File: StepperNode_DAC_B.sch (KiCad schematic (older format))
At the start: 0 parts

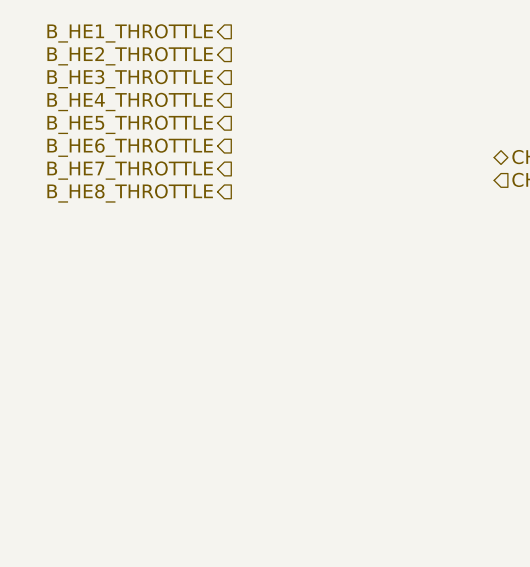
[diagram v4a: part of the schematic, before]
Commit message: Added Aux Prop Interface Sheet
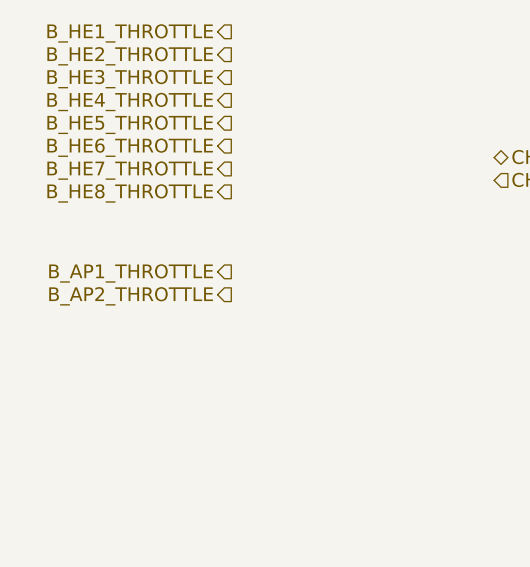
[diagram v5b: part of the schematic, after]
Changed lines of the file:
@@
 $Descr A3 16535 11693
 encoding utf-8
-Sheet 6 14
+Sheet 6 16
 Title "DAC Channel B"
 Date ""
@@
 Text HLabel 2950 3850 2    60   Input ~ 0
 CHB_DAC_NCNVT
+Text HLabel 1800 5200 0    60   Output ~ 0
+B_AP1_THROTTLE
+Text HLabel 1800 5300 0    60   Output ~ 0
+B_AP2_THROTTLE
 $EndSCHEMATC

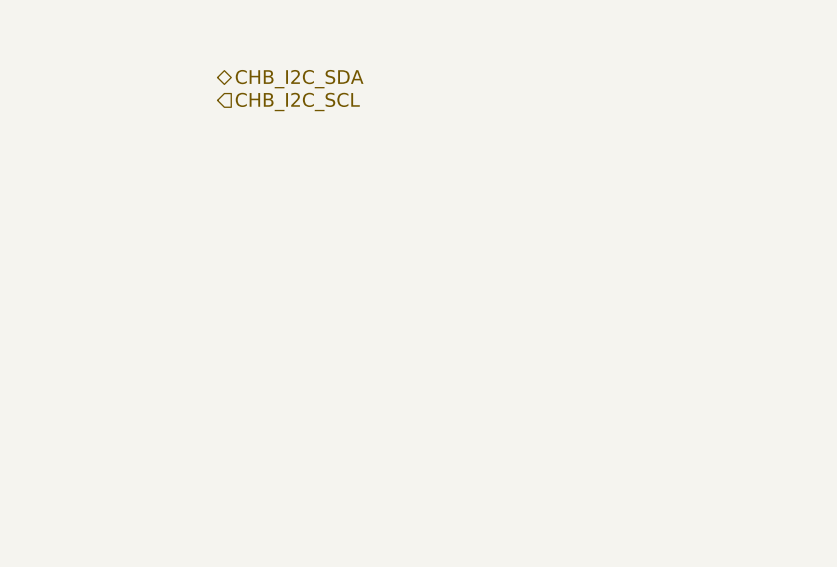
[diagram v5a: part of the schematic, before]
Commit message: Added sheet for Stepper Motor RTD temp sensors.
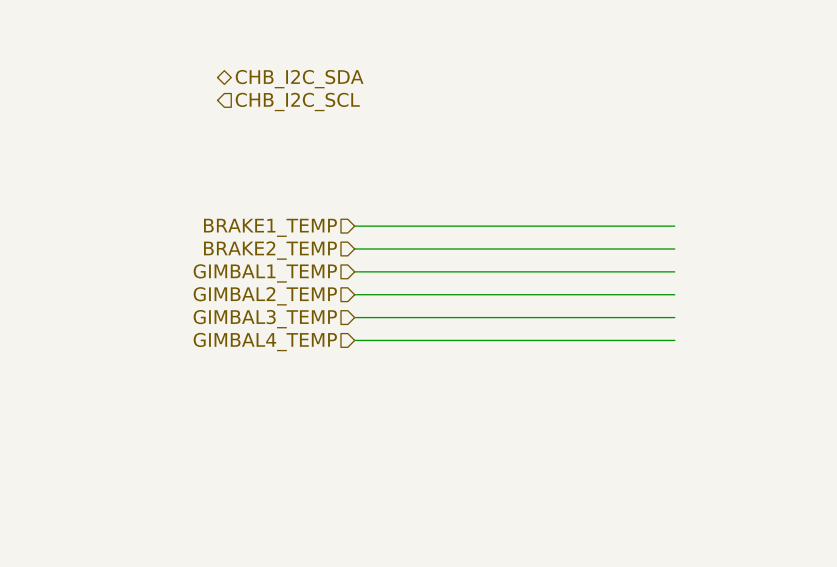
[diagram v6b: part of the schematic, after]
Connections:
- net labels added: BRAKE1_TEMP, BRAKE2_TEMP, GIMBAL1_TEMP, GIMBAL2_TEMP, GIMBAL3_TEMP, GIMBAL4_TEMP
- wire segments 0 -> 6
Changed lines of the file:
@@
 LIBS:microcontrollers
 LIBS:dsp
-LIBS:microchip
 LIBS:analog_switches
 LIBS:motorola
@@
 $Descr A3 16535 11693
 encoding utf-8
-Sheet 6 16
+Sheet 5 17
 Title "DAC Channel B"
 Date ""
@@
 Text HLabel 1800 5300 0    60   Output ~ 0
 B_AP2_THROTTLE
+Wire Wire Line
+	4950 5350 3550 5350
+Text HLabel 3550 5350 0    60   Input ~ 0
+BRAKE1_TEMP
+Wire Wire Line
+	4950 5450 3550 5450
+Text HLabel 3550 5450 0    60   Input ~ 0
+BRAKE2_TEMP
+Wire Wire Line
+	4950 5550 3550 5550
+Text HLabel 3550 5550 0    60   Input ~ 0
+GIMBAL1_TEMP
+Wire Wire Line
+	4950 5650 3550 5650
+Text HLabel 3550 5650 0    60   Input ~ 0
+GIMBAL2_TEMP
+Wire Wire Line
+	4950 5750 3550 5750
+Text HLabel 3550 5750 0    60   Input ~ 0
+GIMBAL3_TEMP
+Wire Wire Line
+	4950 5850 3550 5850
+Text HLabel 3550 5850 0    60   Input ~ 0
+GIMBAL4_TEMP
 $EndSCHEMATC

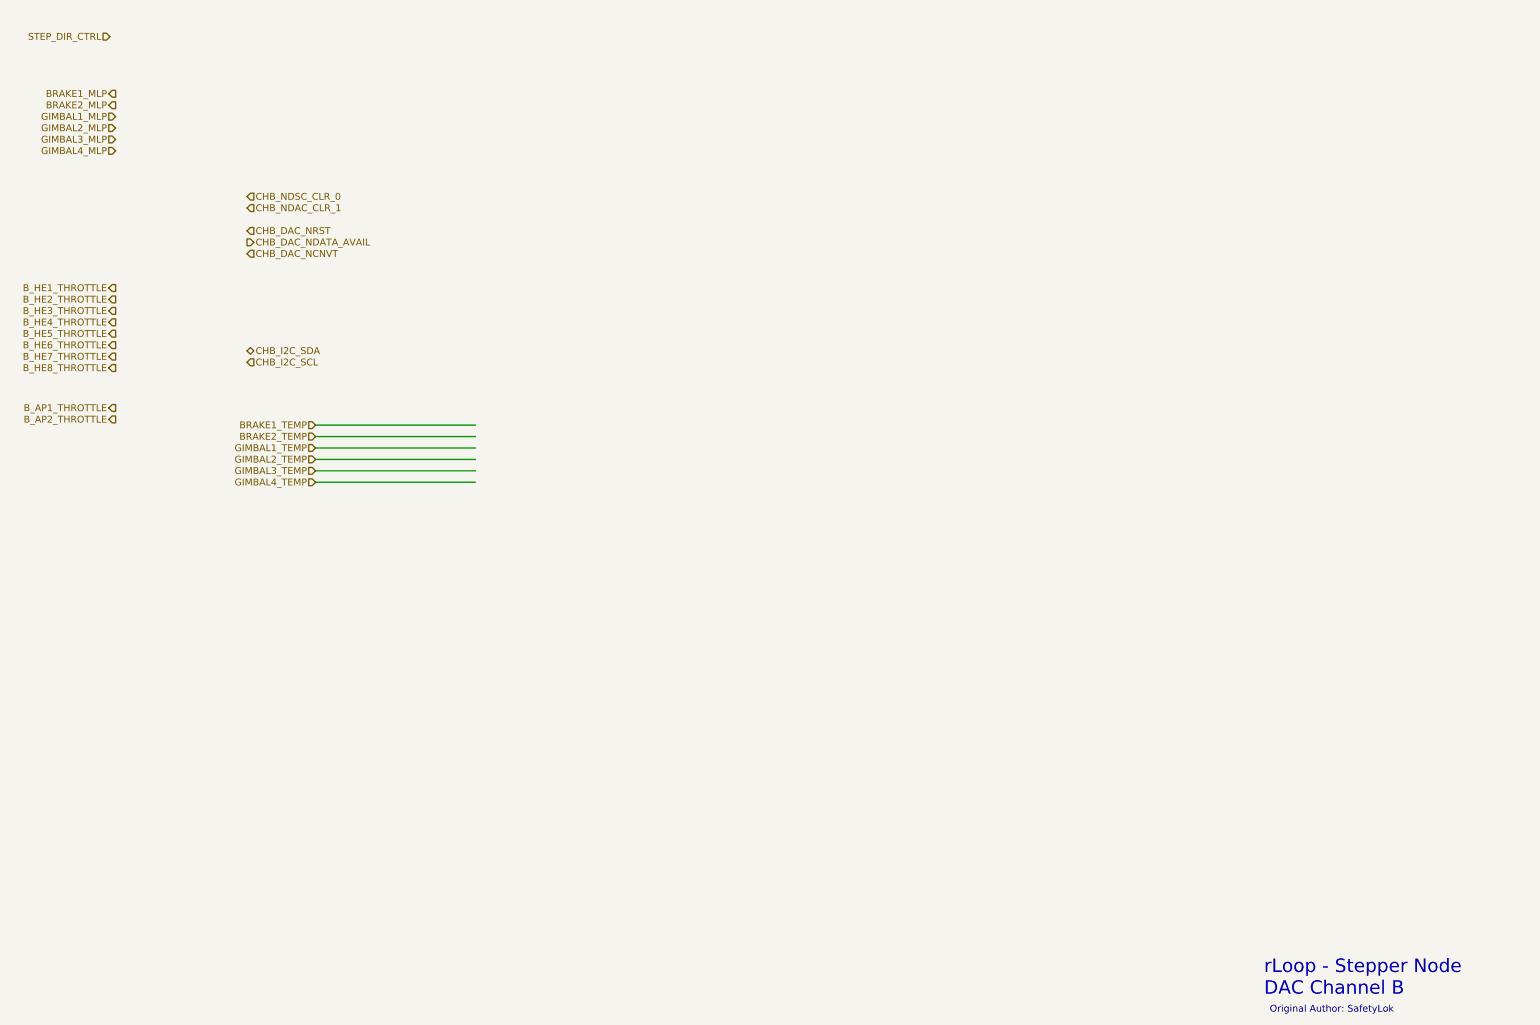
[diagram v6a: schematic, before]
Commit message: Finished DAC interface sheets.
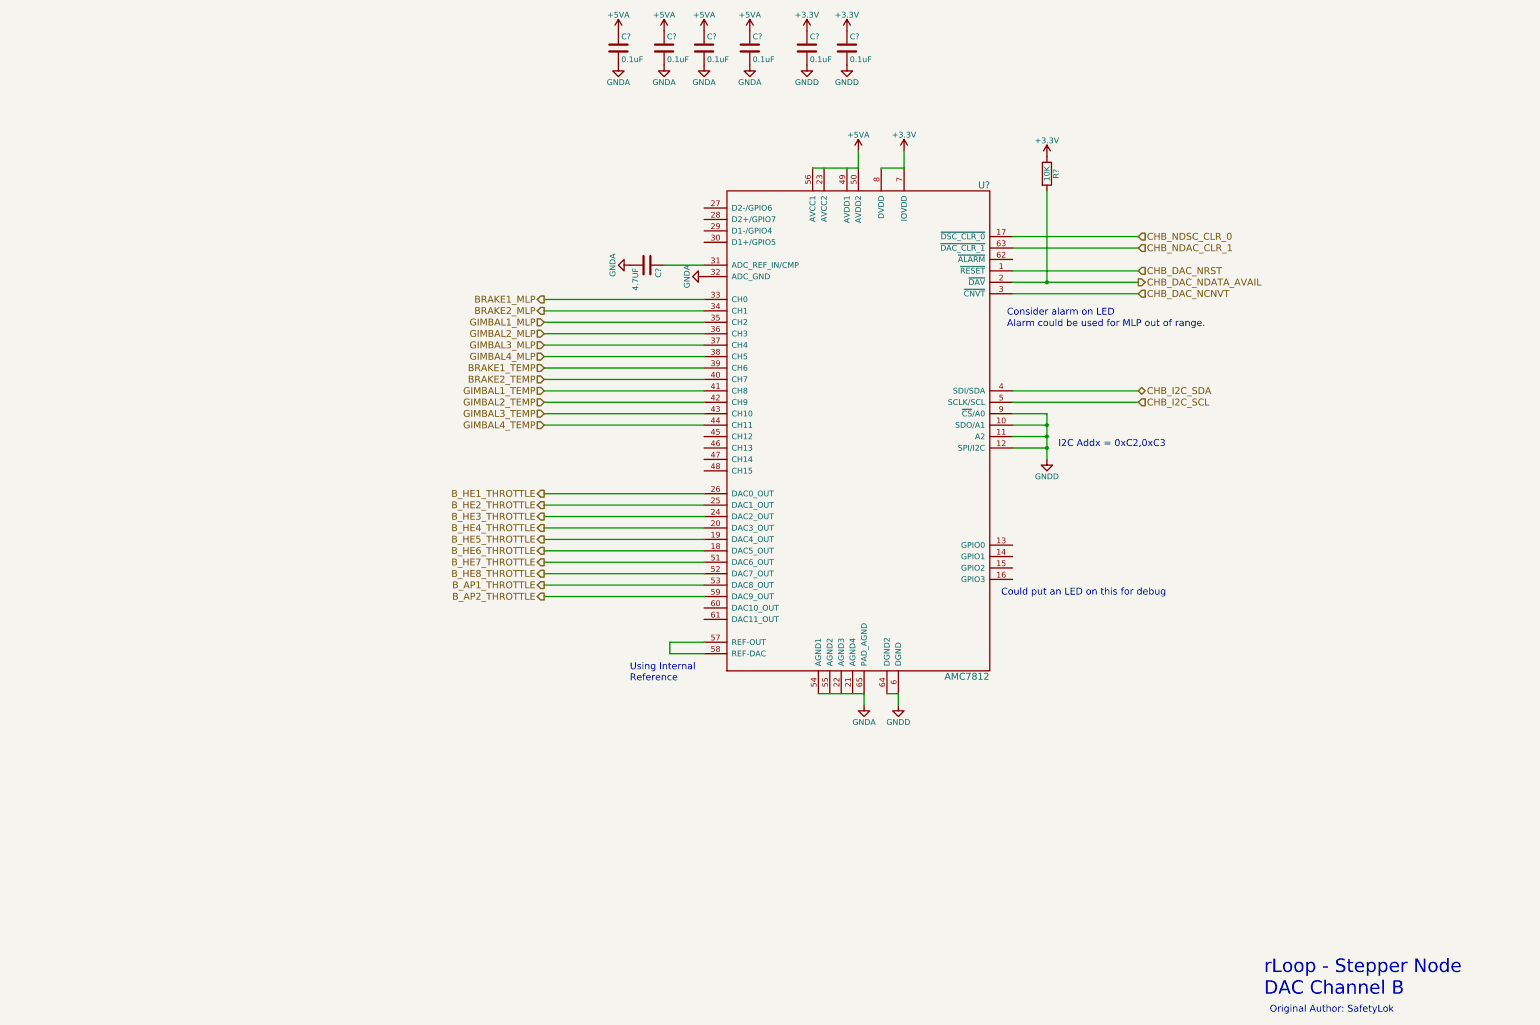
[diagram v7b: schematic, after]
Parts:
- added C?: 4.7UF, symbol C
- added C? (x6): 0.1uF, symbol C
- added R?: 10K, symbol R
- added U?: AMC7812, symbol AMC7812
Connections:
- net labels added: +3.3V, +5VA, GNDA, GNDD
- net labels removed: STEP_DIR_CTRL
- wire segments 6 -> 47
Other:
- note added: "Alarm could be used for MLP out of range."
- note added: "Consider alarm on LED"
- note added: "Could put an LED on this for debug"
- note added: "I2C Addx = 0xC2,0xC3"
- note added: "Using Internal\nReference"

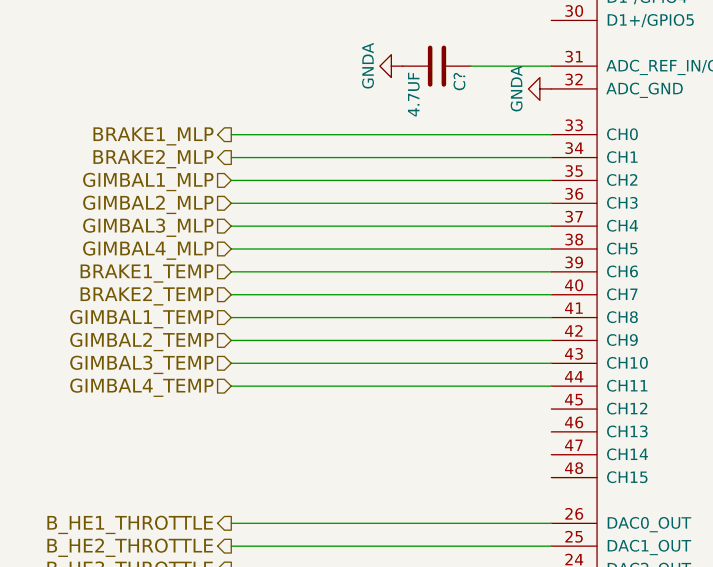
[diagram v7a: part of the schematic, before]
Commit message: Remove Gimbal Functions
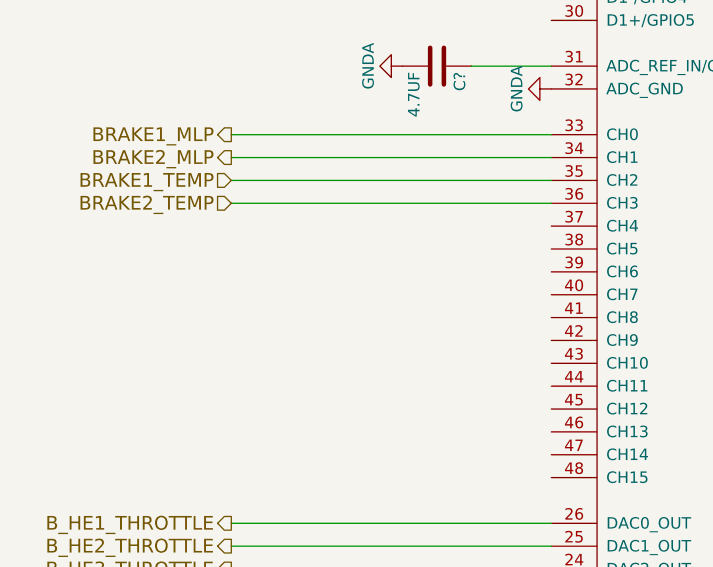
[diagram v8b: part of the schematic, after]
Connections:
- net GIMBAL1_MLP is gone; now on net BRAKE1_TEMP: U?.35 (CH2)
- net GIMBAL2_MLP is gone; now on net BRAKE2_TEMP: U?.36 (CH3)
- net BRAKE1_TEMP: no longer U?.39 (CH6)
- net BRAKE2_TEMP: no longer U?.40 (CH7)
- net GIMBAL1_TEMP: no longer names the net of U?.41 (CH8)
- net GIMBAL2_TEMP: no longer names the net of U?.42 (CH9)
- net GIMBAL3_MLP: no longer names the net of U?.37 (CH4)
- net GIMBAL3_TEMP: no longer names the net of U?.43 (CH10)
- net GIMBAL4_MLP: no longer names the net of U?.38 (CH5)
- net GIMBAL4_TEMP: no longer names the net of U?.44 (CH11)
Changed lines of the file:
@@
 $Descr A3 16535 11693
 encoding utf-8
-Sheet 5 17
+Sheet 16 15
 Title "DAC Channel B"
 Date ""
@@
 Text HLabel 5550 4350 0    60   Output ~ 0
 BRAKE2_MLP
-Text HLabel 5550 4450 0    60   Input ~ 0
-GIMBAL1_MLP
-Text HLabel 5550 4550 0    60   Input ~ 0
-GIMBAL2_MLP
-Text HLabel 5550 4650 0    60   Input ~ 0
-GIMBAL3_MLP
-Text HLabel 5550 4750 0    60   Input ~ 0
-GIMBAL4_MLP
 Text HLabel 5550 5950 0    60   Output ~ 0
 B_HE1_THROTTLE
@@
 Text HLabel 5550 6850 0    60   Output ~ 0
 B_AP2_THROTTLE
-Text HLabel 5550 4850 0    60   Input ~ 0
+Text HLabel 5550 4450 0    60   Input ~ 0
 BRAKE1_TEMP
-Text HLabel 5550 4950 0    60   Input ~ 0
+Text HLabel 5550 4550 0    60   Input ~ 0
 BRAKE2_TEMP
-Text HLabel 5550 5050 0    60   Input ~ 0
-GIMBAL1_TEMP
-Text HLabel 5550 5150 0    60   Input ~ 0
-GIMBAL2_TEMP
-Text HLabel 5550 5250 0    60   Input ~ 0
-GIMBAL3_TEMP
-Text HLabel 5550 5350 0    60   Input ~ 0
-GIMBAL4_TEMP
 $Comp
 L AMC7812 U?
@@
 	5550 4550 6950 4550
 Wire Wire Line
-	6950 4650 5550 4650
-Wire Wire Line
-	6950 4750 5550 4750
-Wire Wire Line
 	6950 5950 5550 5950
 Wire Wire Line
@@
 	6950 6650 5550 6650
 Wire Wire Line
-	6950 4850 5550 4850
-Wire Wire Line
-	6950 4950 5550 4950
-Wire Wire Line
-	6950 5050 5550 5050
-Wire Wire Line
-	6950 5150 5550 5150
-Wire Wire Line
-	6950 5250 5550 5250
-Wire Wire Line
-	6950 5350 5550 5350
-Wire Wire Line
 	6950 6750 5550 6750
